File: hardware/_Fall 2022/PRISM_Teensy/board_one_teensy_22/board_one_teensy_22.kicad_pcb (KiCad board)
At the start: 2 copper layers, 14 parts, among them J1 EAST, J2 CORE_IO, J3 USB_micro, U1 Teensy4.1, U2 BNO055_Breakout, U3 3966

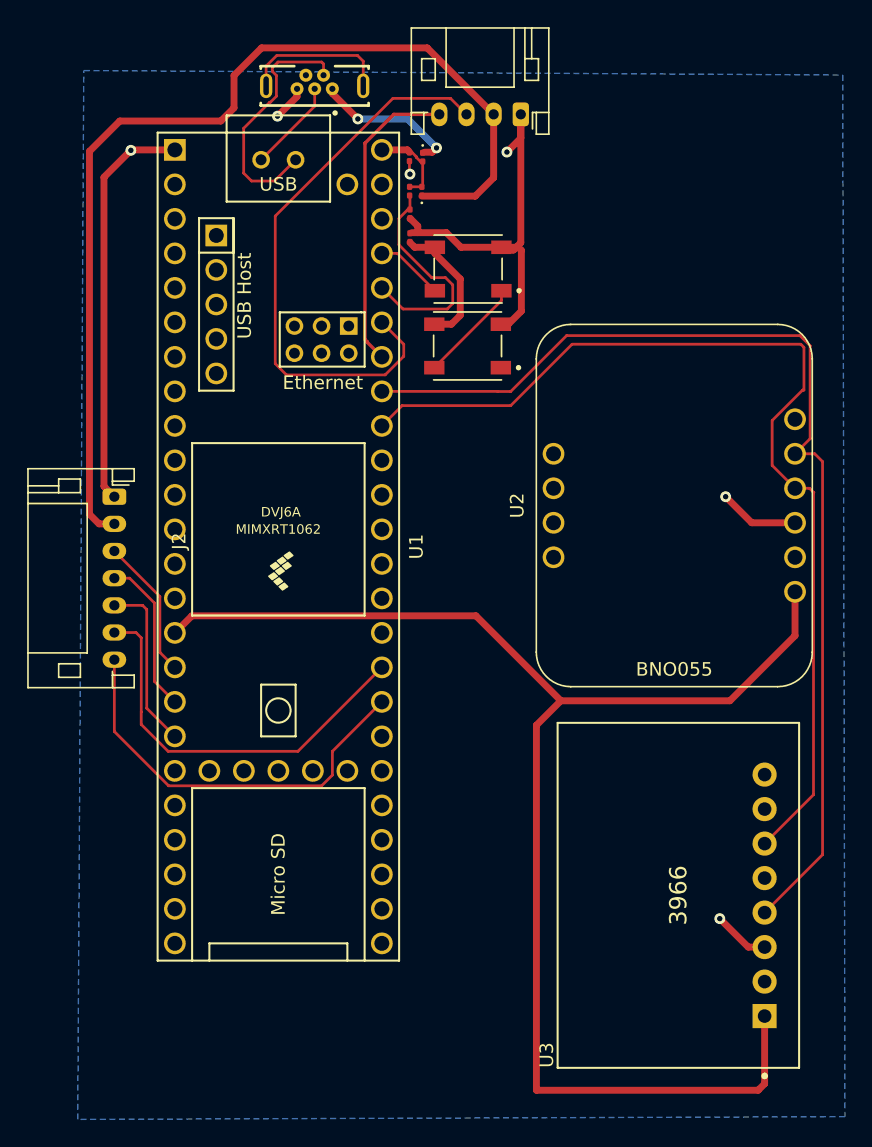
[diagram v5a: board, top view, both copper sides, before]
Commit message: Relocate USB-micro on main Teensy
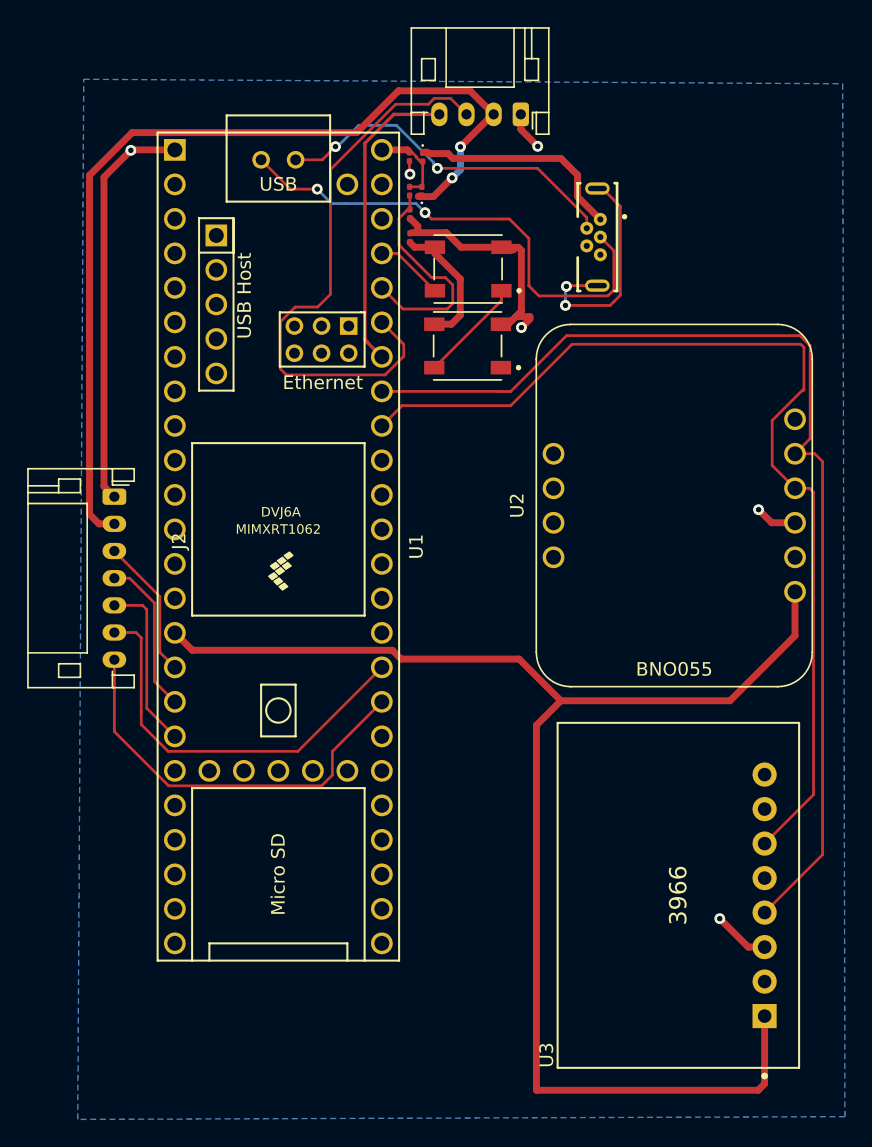
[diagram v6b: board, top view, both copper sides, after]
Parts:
- moved J3 23.6 mm to (156.0, 66.6), turned to -90 degrees
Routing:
- net Net-(J3-Pad3): track 6.86 -> 36.6 mm, vias 0 -> 2
- net GND: track 74.2 -> 60.3 mm
- net Net-(J3-Pad2): track 18.5 -> 26.2 mm, vias 0 -> 2
- net /V_BATT: track 75.7 -> 69.4 mm, vias 0 -> 2
- net unconnected-(J3-PadS1): track 10.9 -> 16.9 mm, vias 0 -> 2
- net /V_USB: track 10.7 -> 15.9 mm, vias 2 -> 0
- net /3.3V: track 105.4 -> 104.4 mm

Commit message: Rough layout of main teensy board
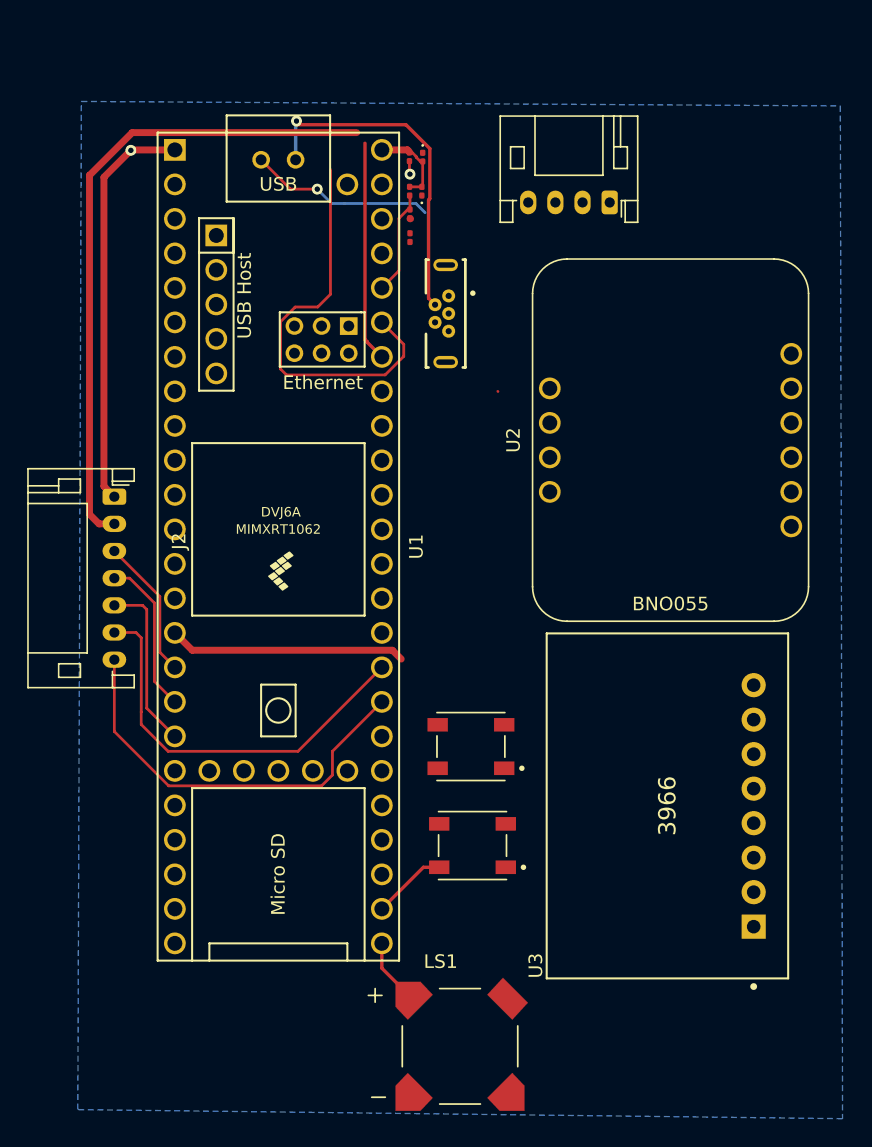
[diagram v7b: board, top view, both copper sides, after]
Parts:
- added LS1: SMT-0827-S-HT-R, buzzer:XDCR_SMT-0827-S-HT-R, F.Cu at (145.8, 126.2)
- moved D4 42.5 mm to (146.8, 111.4)
- moved D5 29.5 mm to (146.7, 104.1)
- moved J3 12.5 mm to (144.8, 72.2)
- moved J1 9.21 mm to (156.9, 64.1)
- moved U3 6.63 mm to (161.1, 108.5)
- moved U2 4.82 mm to (161.3, 81.6)
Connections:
- U1 pad 25: unconnected-(U1-Pad25) -> /BUZZER
- U1 pad 26: unconnected-(U1-Pad26) -> /NEOPIXEL
- U1 pad 37: /BUZZER -> unconnected-(U1-Pad37)
- U1 pad 45: /NEOPIXEL -> unconnected-(U1-Pad45)
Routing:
- net /3.3V: track 104.4 -> 17.5 mm
- net /SCL 0: track 79.2 -> 0.00 mm
- net /SDA 0: track 74.6 -> 0.00 mm
- net GND: track 60.3 -> 30.9 mm, vias 6 -> 2
- net Net-(J3-Pad3): track 36.6 -> 13.7 mm, vias 2 -> 1
- net /V_BATT: track 69.4 -> 48.1 mm, vias 2 -> 0
- net unconnected-(J3-PadS1): track 16.9 -> 0.00 mm, vias 2 -> 0
- net /V_USB: track 15.9 -> 0.00 mm
- net /TX 0: track 42.8 -> 30.2 mm
- net +3.3V: track 9.95 -> 0.00 mm
- net Net-(R4-Pad2): track 16.7 -> 7.76 mm
- net Net-(D4-Pad1): track 7.71 -> 0.00 mm
- net /RX 0: track 22.6 -> 16.2 mm
- net /BUZZER: track 0.00 -> 4.87 mm
- net Net-(J3-Pad2): track 26.2 -> 25.4 mm, vias 2 -> 1

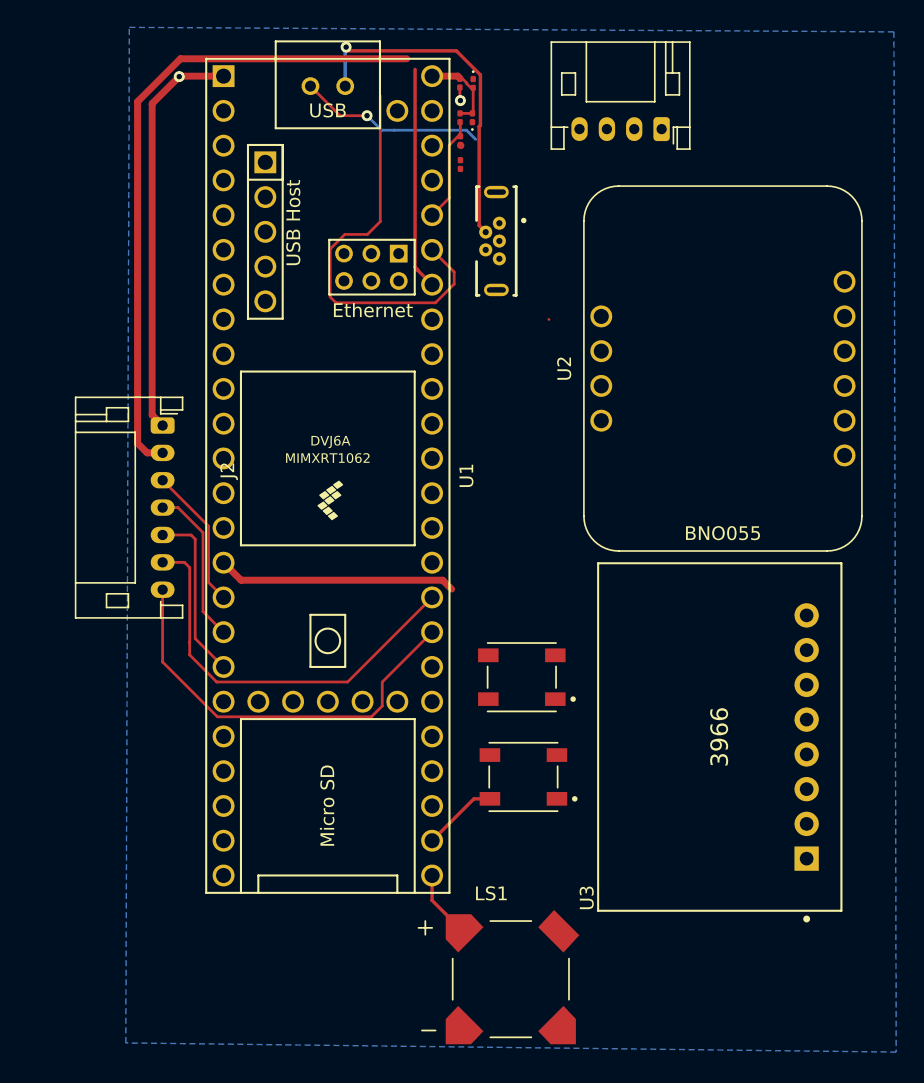
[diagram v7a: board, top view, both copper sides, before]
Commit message: Add rough layout arrangement
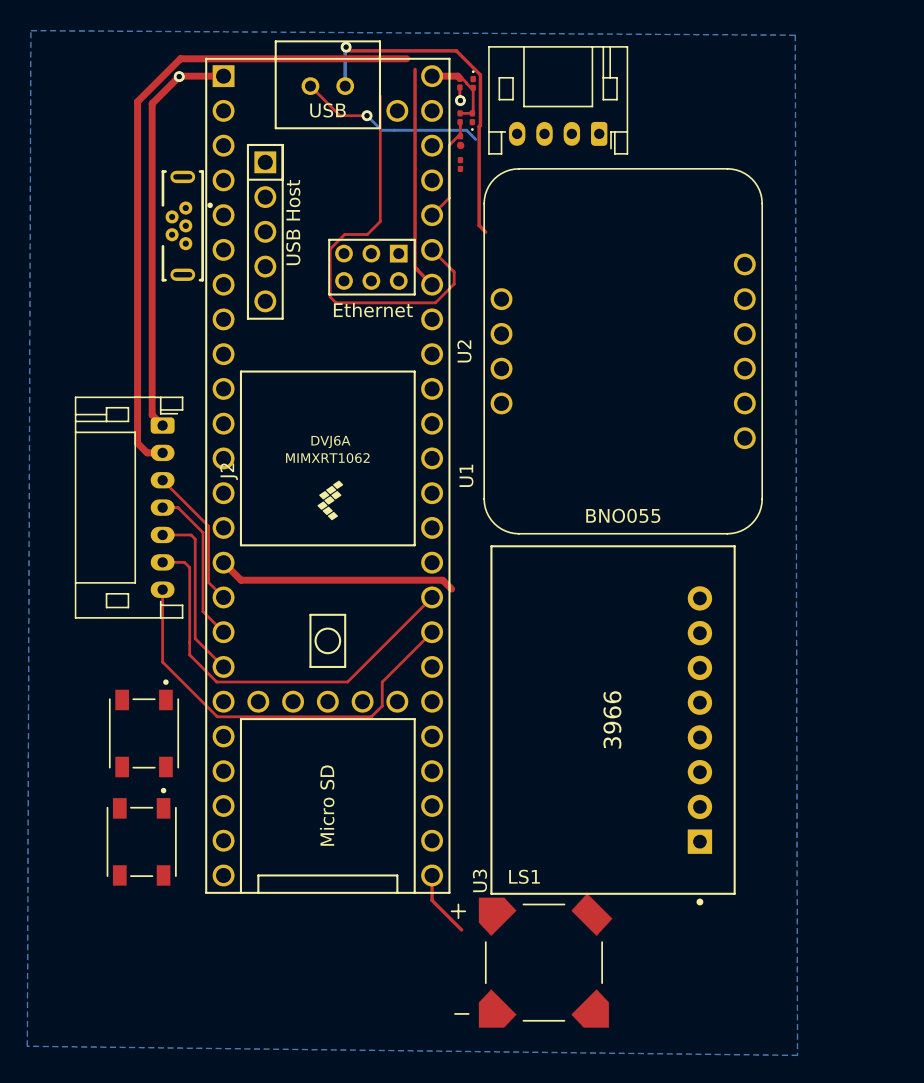
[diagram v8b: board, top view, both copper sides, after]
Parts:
- moved D4 28.3 mm to (118.9, 116.2), turned to -90 degrees
- moved D5 27.9 mm to (119.0, 108.2), turned to -90 degrees
- moved J3 22.9 mm to (121.9, 71.1)
- moved U3 7.90 mm to (153.3, 107.2)
- moved U2 7.40 mm to (154.1, 80.3)
- moved J1 4.57 mm to (152.3, 64.4)
- moved LS1 2.71 mm to (148.3, 125.0)
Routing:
- net /NEOPIXEL: track 5.49 -> 0.00 mm
